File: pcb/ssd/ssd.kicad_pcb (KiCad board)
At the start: 2 copper layers, 61 parts, among them J101 GCT USB4105-GF-A, J102 SWD / 电压参考, J301 NTC 接口 / XH 2.50mm, J302 BTL-004A / XH 2.50mm, Q201 BSS138, Q202 BSS138, SW101 启动（BOOT）, SW102 复位（RESET）, SW301 单位切换, U101 AP2112K-3.3TRG1, U201 HT16K33 / SOP28, U301 SN74LVC1G17DCKR, U401 STM32C562CET6, Y401 24MHz / CL=10pF

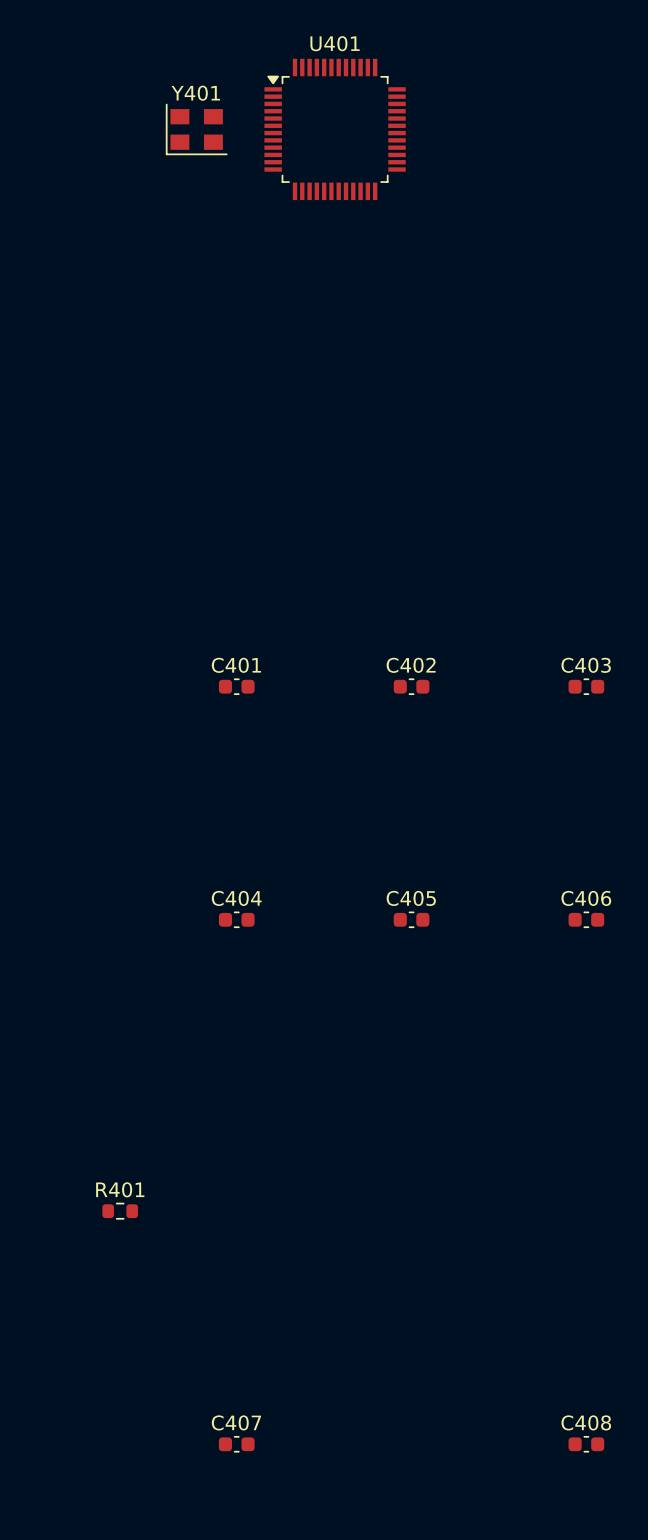
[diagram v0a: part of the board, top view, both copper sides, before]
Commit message: 调整 MCU 周边器件暂放位置
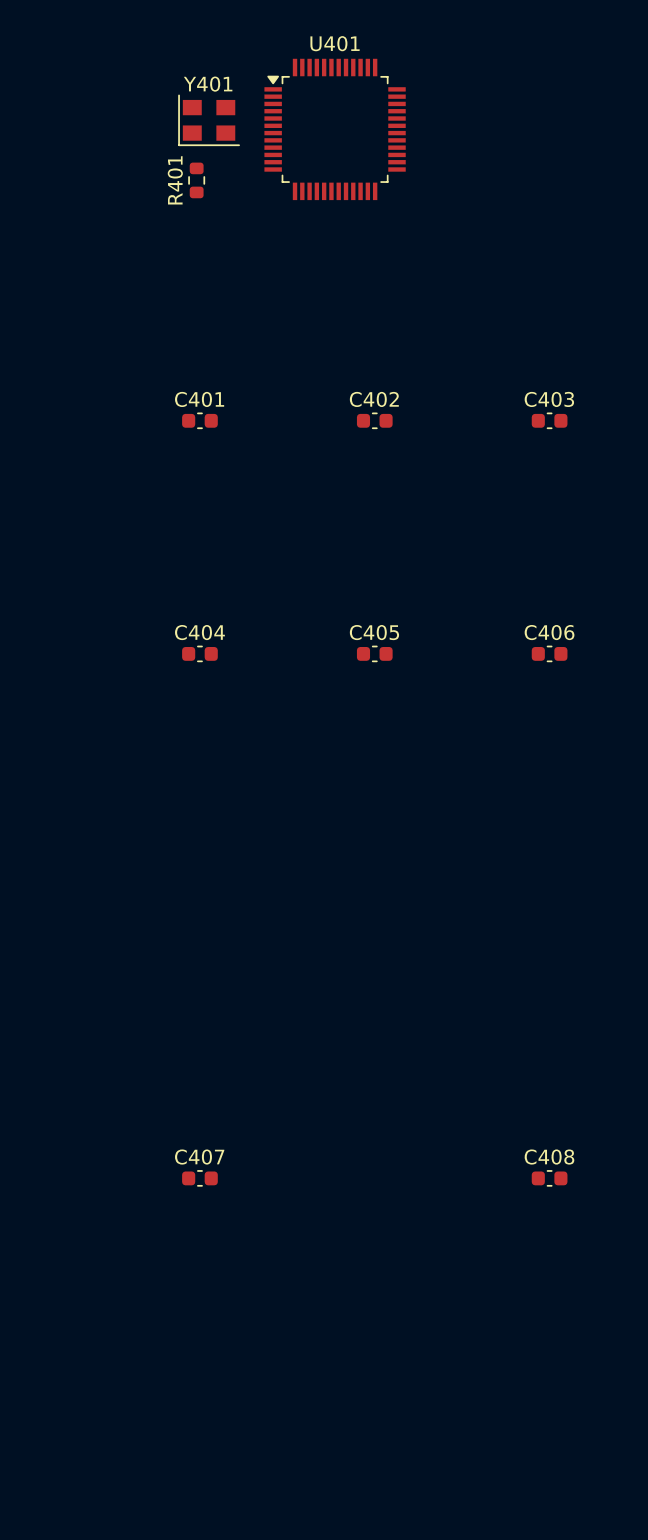
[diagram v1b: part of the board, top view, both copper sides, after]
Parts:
- moved R401 70.9 mm to (336.5, 28.0), turned to 90 degrees
- moved C401 18.4 mm to (336.7, 44.5)
- moved C402 18.4 mm to (348.7, 44.5)
- moved C403 18.4 mm to (360.7, 44.5)
- moved C404 18.4 mm to (336.7, 60.5)
- moved C405 18.4 mm to (348.7, 60.5)
- moved C406 18.4 mm to (360.7, 60.5)
- moved C407 18.4 mm to (336.7, 96.5)
- moved C408 18.4 mm to (360.7, 96.5)
- moved Y401 1.06 mm to (337.4, 23.9)
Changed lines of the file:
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@@
 	(footprint "SSD:Capacitor_SMD__C_0603_1608Metric"
 		(layer "F.Cu")
-		(at 339.25 62.75)
+		(at 336.725 44.5)
 		(descr "Capacitor SMD 0603 (1608 Metric), square (rectangular) end terminal, IPC-7351 nominal, (Body size source: IPC-SM-782 page 76, https://www.pcb-3d.com/wordpress/wp-content/uploads/ipc-sm-782a_amendment_1_and_2.pdf)")
 		(tags "capacitor")
@@
 	(footprint "SSD:Abracon_ABM8_3.2x2.5mm"
 		(layer "F.Cu")
-		(at 336.5 24.5)
+		(at 337.35 23.875)
 		(descr "Abracon ABM8；3.2×2.5mm；焊盘1.30×1.05mm，中心距2.30×1.75mm；1/3晶体端，2/4外壳接地。")
 		(property "Reference" "Y401"
@@
 	(footprint "SSD:Capacitor_SMD__C_0603_1608Metric"
 		(layer "F.Cu")
-		(at 339.25 114.75)
+		(at 336.725 96.5)
 		(descr "Capacitor SMD 0603 (1608 Metric), square (rectangular) end terminal, IPC-7351 nominal, (Body size source: IPC-SM-782 page 76, https://www.pcb-3d.com/wordpress/wp-content/uploads/ipc-sm-782a_amendment_1_and_2.pdf)")
 		(tags "capacitor")
@@
 	(footprint "SSD:Capacitor_SMD__C_0603_1608Metric"
 		(layer "F.Cu")
-		(at 363.25 114.75)
+		(at 360.725 96.5)
 		(descr "Capacitor SMD 0603 (1608 Metric), square (rectangular) end terminal, IPC-7351 nominal, (Body size source: IPC-SM-782 page 76, https://www.pcb-3d.com/wordpress/wp-content/uploads/ipc-sm-782a_amendment_1_and_2.pdf)")
 		(tags "capacitor")
@@
 	(footprint "SSD:Capacitor_SMD__C_0603_1608Metric"
 		(layer "F.Cu")
-		(at 351.25 62.75)
+		(at 348.725 44.5)
 		(descr "Capacitor SMD 0603 (1608 Metric), square (rectangular) end terminal, IPC-7351 nominal, (Body size source: IPC-SM-782 page 76, https://www.pcb-3d.com/wordpress/wp-content/uploads/ipc-sm-782a_amendment_1_and_2.pdf)")
 		(tags "capacitor")
@@
 	(footprint "SSD:Resistor_SMD__R_0603_1608Metric"
 		(layer "F.Cu")
-		(at 331.25 98.75)
+		(at 336.5 28 90)
 		(descr "Resistor SMD 0603 (1608 Metric), square (rectangular) end terminal, IPC-7351 nominal, (Body size source: IPC-SM-782 page 72, https://www.pcb-3d.com/wordpress/wp-content/uploads/ipc-sm-782a_amendment_1_and_2.pdf)")
 		(tags "resistor")
 		(property "Reference" "R401"
-			(at 0 -1.43 0)
+			(at 0 -1.43 90)
 			(layer "F.SilkS")
 			(effects
@@
 		)
 		(property "Value" "0R"
-			(at 0 1.43 0)
+			(at 0 1.43 90)
 			(layer "F.Fab")
 			(hide yes)
@@
 		)
 		(property "Datasheet" ""
-			(at 0 0 0)
+			(at 0 0 90)
 			(layer "F.Fab")
 			(hide yes)
@@
 		)
 		(property "Description" ""
-			(at 0 0 0)
+			(at 0 0 90)
 			(layer "F.Fab")
 			(hide yes)
@@
 		)
 		(property "KiLib_Generator" "SMD_2terminal_chip_molded"
-			(at 0 0 0)
+			(at 0 0 90)
 			(layer "F.SilkS")
 			(hide yes)
@@
 		)
 		(fp_text user "${REFERENCE}"
-			(at 0 0 0)
+			(at 0 0 90)
 			(layer "F.Fab")
 			(effects
@@
 		)
 		(pad "1" smd roundrect
-			(at -0.825 0)
+			(at -0.825 0 90)
 			(size 0.8 0.95)
 			(layers "F.Cu" "F.Mask" "F.Paste")
@@
 		)
 		(pad "2" smd roundrect
-			(at 0.825 0)
+			(at 0.825 0 90)
 			(size 0.8 0.95)
 			(layers "F.Cu" "F.Mask" "F.Paste")
@@
 	(footprint "SSD:Capacitor_SMD__C_0603_1608Metric"
 		(layer "F.Cu")
-		(at 363.25 78.75)
+		(at 360.725 60.5)
 		(descr "Capacitor SMD 0603 (1608 Metric), square (rectangular) end terminal, IPC-7351 nominal, (Body size source: IPC-SM-782 page 76, https://www.pcb-3d.com/wordpress/wp-content/uploads/ipc-sm-782a_amendment_1_and_2.pdf)")
 		(tags "capacitor")
@@
 	(footprint "SSD:Capacitor_SMD__C_0603_1608Metric"
 		(layer "F.Cu")
-		(at 363.25 62.75)
+		(at 360.725 44.5)
 		(descr "Capacitor SMD 0603 (1608 Metric), square (rectangular) end terminal, IPC-7351 nominal, (Body size source: IPC-SM-782 page 76, https://www.pcb-3d.com/wordpress/wp-content/uploads/ipc-sm-782a_amendment_1_and_2.pdf)")
 		(tags "capacitor")
@@
 	(footprint "SSD:Capacitor_SMD__C_0603_1608Metric"
 		(layer "F.Cu")
-		(at 351.25 78.75)
+		(at 348.725 60.5)
 		(descr "Capacitor SMD 0603 (1608 Metric), square (rectangular) end terminal, IPC-7351 nominal, (Body size source: IPC-SM-782 page 76, https://www.pcb-3d.com/wordpress/wp-content/uploads/ipc-sm-782a_amendment_1_and_2.pdf)")
 		(tags "capacitor")
@@
 	(footprint "SSD:Capacitor_SMD__C_0603_1608Metric"
 		(layer "F.Cu")
-		(at 339.25 78.75)
+		(at 336.725 60.5)
 		(descr "Capacitor SMD 0603 (1608 Metric), square (rectangular) end terminal, IPC-7351 nominal, (Body size source: IPC-SM-782 page 76, https://www.pcb-3d.com/wordpress/wp-content/uploads/ipc-sm-782a_amendment_1_and_2.pdf)")
 		(tags "capacitor")

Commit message: 更新PCB与3D模型并整理工程文档
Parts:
- removed J102: SWD / 电压参考, SSD:Connector_PinHeader_2.54mm__PinHeader_1x05_P2.54mm_Vertical
- removed R401: 0R, SSD:Resistor_SMD__R_0603_1608Metric
- C407, C408: value 12p / C0G -> 6.8p / C0G
- moved C403 221.4 mm to (160.5, 139.0)
- moved U401 215.5 mm to (157.0, 128.0)
- moved Y401 214.6 mm to (149.3, 127.3), turned to -90 degrees
- moved C408 214.1 mm to (149.3, 130.3), turned to 180 degrees
- moved C406 213.4 mm to (160.5, 134.5)
- moved C402 209.9 mm to (160.5, 137.5)
- moved C405 204.6 mm to (158.3, 135.3), turned to -90 degrees
- moved C401 198.5 mm to (160.5, 136.0)
- moved C404 193.5 mm to (160.5, 140.5)
- moved C407 189.5 mm to (149.3, 124.3)
- moved SW301 131.8 mm to (142.7, 117.6), turned to 90 degrees
- moved R305 116.8 mm to (144.8, 111.3), turned to -90 degrees
- moved U301 112.4 mm to (134.7, 129.3)
- moved R210 111.2 mm to (163.0, 65.1), turned to 180 degrees
- moved C301 109.9 mm to (138.5, 120.5), turned to 90 degrees
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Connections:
- C407 pad 1: /STM32C562 最小系统/HSE_X -> Net-(U401-PH0-OSC_IN)
- C408 pad 1: /STM32C562 最小系统/HSE_IN -> Net-(U401-PH1-OSC_OUT)
- U401 pad 5: /STM32C562 最小系统/HSE_IN -> Net-(U401-PH0-OSC_IN)
- U401 pad 6: /STM32C562 最小系统/HSE_OUT -> Net-(U401-PH1-OSC_OUT)
- Y401 pad 1: /STM32C562 最小系统/HSE_X -> Net-(U401-PH0-OSC_IN)
- Y401 pad 3: /STM32C562 最小系统/HSE_IN -> Net-(U401-PH1-OSC_OUT)
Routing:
- net +5V: track 0.00 -> 125.3 mm, vias 0 -> 2
- net +3V3: track 0.00 -> 113.4 mm
- net Net-(DS201-I): track 0.00 -> 66.3 mm
- net Net-(DS201-H): track 0.00 -> 63.1 mm
- net Net-(DS201-COM1): track 0.00 -> 61.4 mm
- net Net-(DS201-COM2): track 0.00 -> 60.9 mm
- net Net-(DS201-COM3): track 0.00 -> 60.3 mm
- net Net-(DS201-COM4): track 0.00 -> 59.8 mm
- net Net-(DS201-COM5): track 0.00 -> 59.3 mm
- net Net-(DS201-COM6): track 0.00 -> 58.7 mm
- net Net-(Q202-D): track 0.00 -> 45.3 mm
- net Net-(U201-ROW9): track 0.00 -> 41.7 mm
- net Net-(Q201-D): track 0.00 -> 34.5 mm
- net Net-(D101-VBUS): track 0.00 -> 29.1 mm
- net NTC_ADC: track 0.00 -> 27.5 mm
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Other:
- board outline added: 88 x 105.5 mm
- board text removed: "A2 封装暂放 · STM32C562CET6 / 24MHz 外部晶振 · 尚未布线"
- board text removed: "DS201：直径 58mm，须实物对位"
- board text removed: "HT16K33 与显示驱动"
- board text removed: "USB-C 接口、电源与调试"
- board text removed: "温度、流量与用户按键"
- board text removed: "电阻、电容均为 0603（1608 公制）；尚未绘制板框和走线。"

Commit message: 更新硬件设计
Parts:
- added C105: 22u / 10V, SSD:Capacitor_SMD__C_1206_3216Metric, F.Cu at (212.6, 142.4)
- added C106: 100n, SSD:Capacitor_SMD__C_0603_1608Metric, F.Cu at (222.8, 142.0)
- added C107: 22u / 10V, SSD:Capacitor_SMD__C_1206_3216Metric, F.Cu at (212.6, 145.8)
- added C108: 22u / 10V, SSD:Capacitor_SMD__C_1206_3216Metric, F.Cu at (212.6, 149.1)
- added C109: 100n, SSD:Capacitor_SMD__C_0603_1608Metric, F.Cu at (222.8, 144.5)
- added C110: 10u / 35V, SSD:Capacitor_SMD__C_1206_3216Metric, F.Cu at (212.6, 152.4)
- added L101: 3.9u / 3A, SSD:Inductor_Sunlord_SWPA4030S, F.Cu at (218.0, 143.5)
- added L102: 4.7u / 2.9A, SSD:Inductor_Sunlord_SWPA4030S, F.Cu at (218.0, 149.1)
- added U102: AP63205WU-7, SSD:Package_TO_SOT_SMD__SOT-23-6, F.Cu at (217.8, 154.2)
- C101: value 1u / 10V -> 100n / 25V
- C102: value 1u / 10V -> 10u / 35V; footprint SSD:Capacitor_SMD__C_0603_1608Metric -> SSD:Capacitor_SMD__C_1206_3216Metric
- C103: value 4.7u / 10V -> 22u / 10V; footprint SSD:Capacitor_SMD__C_0603_1608Metric -> SSD:Capacitor_SMD__C_1206_3216Metric
- DS201: moved to B.Cu
- F101: value 500mA 保持电流 -> 0.5A / 24V
- U101: value AP2112K-3.3TRG1 -> AP63203WU-7; footprint SSD:Package_TO_SOT_SMD__SOT-23-5 -> SSD:Package_TO_SOT_SMD__SOT-23-6
- moved R201 96.4 mm to (69.7, 91.8)
- moved R202 96.4 mm to (69.7, 94.3)
- moved R203 96.4 mm to (69.6, 96.9)
- moved R204 96.4 mm to (69.7, 99.5)
- moved R205 96.4 mm to (69.7, 102.1)
- moved R206 96.4 mm to (69.7, 104.8)
- moved R207 96.4 mm to (69.6, 107.0)
- moved R210 96.4 mm to (69.7, 89.3)
- moved U201 88.4 mm to (79.2, 97.8), turned to 180 degrees
- moved U101 67.5 mm to (226.1, 128.4), turned to 180 degrees
- moved D101 64.1 mm to (229.5, 133.0)
- moved F101 63.3 mm to (232.0, 129.1), turned to 90 degrees
- moved C102 61.7 mm to (229.5, 129.0), turned to -90 degrees
- moved J101 59.0 mm to (238.5, 133.1)
- moved R101 59.0 mm to (237.0, 139.6)
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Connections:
- C101 pad 1: +5V -> VIN_SYS
- C102 pad 1: +5V -> VIN_SYS
- D101 pad 5: Net-(D101-VBUS) -> +5V
- F101 pad 1: Net-(D101-VBUS) -> Net-(F101-Pad1)
- F101 pad 2: +5V -> VIN_SYS
- J101 pad A4: Net-(D101-VBUS) -> Net-(F101-Pad1)
- J101 pad A9: Net-(D101-VBUS) -> Net-(F101-Pad1)
- J101 pad B4: Net-(D101-VBUS) -> Net-(F101-Pad1)
- J101 pad B9: Net-(D101-VBUS) -> Net-(F101-Pad1)
- U101 pad 1: +5V -> +3V3
- U101 pad 2: GND -> VIN_SYS
- U101 pad 3: +5V -> VIN_SYS
- U101 pad 4: unconnected-(U101-NC-Pad4) -> GND
- U101 pad 5: +3V3 -> Net-(U101-SW)
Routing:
- net +5V: track 125.3 -> 0.00 mm, vias 2 -> 0
- net +3V3: track 113.4 -> 0.00 mm
- net Net-(DS201-I): track 66.3 -> 0.00 mm
- net Net-(DS201-H): track 63.1 -> 0.00 mm
- net Net-(DS201-COM1): track 61.4 -> 0.84 mm
- net Net-(DS201-COM2): track 60.9 -> 1.02 mm
- net Net-(DS201-COM3): track 60.3 -> 1.02 mm
- net Net-(DS201-COM5): track 59.3 -> 0.00 mm
- net Net-(DS201-COM6): track 58.7 -> 0.00 mm
- net Net-(DS201-COM4): track 59.8 -> 1.74 mm
- net Net-(Q202-D): track 45.3 -> 0.00 mm
- net Net-(U201-ROW9): track 41.7 -> 0.00 mm
- net Net-(Q201-D): track 34.5 -> 0.00 mm
- net Net-(D101-VBUS): track 29.1 -> 0.00 mm
- net NTC_ADC: track 27.5 -> 0.00 mm
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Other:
- board outline removed
